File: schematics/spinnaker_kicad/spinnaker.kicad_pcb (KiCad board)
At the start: 2 copper layers, 138 parts, among them J1 Conn_01x02, J2 Conn_01x02, J3 Conn_01x02, J4 Conn_01x02, J5 Jack-DC, J6 Conn_01x08, J7 Conn_01x02, J8 Conn_01x02, J9 Conn_01x02, Q1 AO3401, U1 SpinSemi_FV-1, U10 24LC32, U11 24LC32, U12 24LC32, U13 24LC32, U14 24LC32, U15 24LC32, U16 24LC32, U17 AMS1117-3.3, U18 AMS1117-5.0, U2 TL071, U3 TL071, U4 TL071, U5 TL071, U6 PT2258, U7 MCP4728, U8 PCF8574, U9 24LC32, Y1 32768Hz

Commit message: Corrección de conexiones no enrutadas
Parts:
- removed J7, J8, J9: Conn_01x02, Connector_JST:JST_GH_BM02B-GHS-TBT_1x02-1MP_P1.25mm_Vertical
- added REF**: MountingHole_2.5mm_Pad_Via, MountingHole:MountingHole_2.5mm_Pad_Via, F.Cu at (107.3, 64.1)
- added REF**: MountingHole_2.5mm_Pad_Via, MountingHole:MountingHole_2.5mm_Pad_Via, F.Cu at (107.3, 112.4)
- added REF**: MountingHole_2.5mm_Pad_Via, MountingHole:MountingHole_2.5mm_Pad_Via, F.Cu at (181.0, 112.4)
- added REF**: MountingHole_2.5mm_Pad_Via, MountingHole:MountingHole_2.5mm_Pad_Via, F.Cu at (181.0, 63.5)
- C44, C45, C46, C47, C48, C49, C50, C51, C52, C53, C55, C56, C57, C59, C60: moved to B.Cu
- D1: footprint LED_THT:LED_Rectangular_W3.0mm_H2.0mm -> Connector_Wire:SolderWire-0.75sqmm_1x02_P4.8mm_D1.25mm_OD2.3mm
- J1, J2, J3, J4: footprint Connectors:1X02_LONGPADS -> Connector_Wire:SolderWire-0.75sqmm_1x02_P4.8mm_D1.25mm_OD2.3mm
- J5: value Jack-DC -> Conn_01x02; footprint Connector_BarrelJack:BarrelJack_Horizontal -> Connector_JST:JST_PH_S2B-PH-SM4-TB_1x02-1MP_P2.00mm_Horizontal
- J6: value Conn_01x08 -> Conn_01x10; footprint Connector_JST:JST_GH_SM08B-GHS-TB_1x08-1MP_P1.25mm_Horizontal -> Connector_JST:JST_SH_SM10B-SRSS-TB_1x10-1MP_P1.00mm_Horizontal
- RV1, RV2: footprint Connectors:1X03_LONGPADS -> Connector_Wire:SolderWire-0.75sqmm_1x02_P4.8mm_D1.25mm_OD2.3mm
- moved R46 95.6 mm to (175.3, 85.7)
- moved C33 95.4 mm to (175.3, 82.5)
- moved Q1 94.4 mm to (174.6, 71.8), turned to 90 degrees
- moved R45 94.4 mm to (170.2, 85.7)
- moved C38 94.2 mm to (170.2, 82.5)
- moved C58 91.6 mm to (175.3, 88.9), turned to 180 degrees
- moved R43 87.1 mm to (170.2, 71.8)
- moved C54 83.1 mm to (170.2, 88.9)
- moved C30 79.2 mm to (172.7, 77.5), turned to 0 degrees
- moved U17 67.8 mm to (172.7, 107.3), turned to 270 degrees
- moved U18 67.7 mm to (172.7, 95.2), turned to 270 degrees
- moved J5 66.5 mm to (172.7, 63.5), turned to 180 degrees
- moved C34 57.1 mm to (170.2, 101.0), turned to 180 degrees
- moved C37 57.1 mm to (175.3, 101.0), turned to 180 degrees
- moved R34 54.0 mm to (160.7, 92.7), turned to 180 degrees
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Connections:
- J6 pad 2: T0 -> +3V3
- J6 pad 3: S2 -> +5V
- J6 pad 4: S1 -> +9V
- J6 pad 5: S0 -> T0
- J6 pad 6: SDA -> S2
- J6 pad 7: SCL -> S1
- J6 pad 8: Earth -> S0
- RV1 pad 1: Net-(R1-Pad1) -> Net-(C5-Pad2)
- RV2 pad 1: Net-(R3-Pad1) -> Net-(C6-Pad2)
- U10 pad 7: Net-(U10-Pad7) -> Earth
- U11 pad 7: Net-(U11-Pad7) -> Earth
- U12 pad 7: Net-(U12-Pad7) -> Earth
- U13 pad 7: Net-(U13-Pad7) -> Earth
- U14 pad 7: Net-(U14-Pad7) -> Earth
- U15 pad 7: Net-(U15-Pad7) -> Earth
- U16 pad 7: Net-(U16-Pad7) -> Earth
- U8 pad 4: Net-(U8-Pad4) -> Net-(U12-Pad1)
- U8 pad 5: Net-(U10-Pad1) -> Net-(U11-Pad1)
- U8 pad 6: Net-(U11-Pad1) -> Net-(U10-Pad1)
- U8 pad 7: Net-(U12-Pad1) -> Net-(U8-Pad7)
- U9 pad 1: Net-(U8-Pad4) -> Net-(U8-Pad7)
- U9 pad 7: Net-(U9-Pad7) -> Earth
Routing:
- net +3V3: track 0.00 -> 276.8 mm, vias 0 -> 20
- net SCL: track 0.00 -> 181.7 mm, vias 0 -> 8
- net +9V: track 0.00 -> 158.5 mm, vias 0 -> 6
- net SDA: track 0.00 -> 154.7 mm, vias 0 -> 7
- net Earth: track 0.00 -> 145.3 mm, vias 0 -> 365
- net 4V5: track 0.00 -> 116.9 mm, vias 0 -> 5
- net +5V: track 0.00 -> 114.2 mm, vias 0 -> 4
- net Net-(U8-Pad7): track 0.00 -> 60.3 mm
- net Net-(U10-Pad1): track 0.00 -> 51.9 mm
- net S0: track 0.00 -> 49.6 mm
- net Net-(U16-Pad1): track 0.00 -> 44.3 mm
- net Net-(U11-Pad1): track 0.00 -> 43.5 mm
- net RIGHT_PREOUT: track 0.00 -> 42.0 mm
- net Net-(C25-Pad1): track 0.00 -> 39.5 mm
- net S2: track 0.00 -> 36.7 mm
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- added copper zone on F.Cu, net Earth
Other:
- board outline added: 83.8 x 59.1 mm

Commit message: Rediseño con SMPS.
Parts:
- removed the REF** at (107.3, 64.1)
- removed the REF** at (107.3, 112.4)
- removed the REF** at (181.0, 112.4)
- removed the REF** at (181.0, 63.5)
- added C61: 100nF, Capacitor_SMD:C_0805_2012Metric, F.Cu at (183.5, 86.4)
- added C62: 22uF, Capacitor_SMD:C_0805_2012Metric, F.Cu at (175.3, 85.7)
- added C63: 100nF, Capacitor_SMD:C_0805_2012Metric, F.Cu at (183.5, 77.5)
- added C64: 22uF, Capacitor_SMD:C_0805_2012Metric, F.Cu at (183.5, 74.9)
- added L1: 6.8uH, Inductor_SMD:L_10.4x10.4_H4.8, F.Cu at (179.7, 93.3)
- added R44: 100K, Resistor_SMD:R_0805_2012Metric, F.Cu at (172.1, 74.9)
- added R48: 40K2, Resistor_SMD:R_0805_2012Metric, F.Cu at (175.9, 77.5)
- added R49: 40K2, Resistor_SMD:R_0805_2012Metric, F.Cu at (175.9, 74.9)
- added R50: 7K68, Resistor_SMD:R_0805_2012Metric, F.Cu at (172.1, 77.5)
- added R51: 4K7, Resistor_SMD:R_0805_2012Metric, B.Cu at (133.3, 81.9)
- added REF**: MountingHole_2.2mm_M2_Pad_Via, MountingHole:MountingHole_2.2mm_M2_Pad_Via, F.Cu at (184.2, 62.2)
- added REF**: MountingHole_2.2mm_M2_Pad_Via, MountingHole:MountingHole_2.2mm_M2_Pad_Via, F.Cu at (184.2, 112.4)
- added REF**: MountingHole_2.2mm_M2_Pad_Via, MountingHole:MountingHole_2.2mm_M2_Pad_Via, F.Cu at (107.3, 112.4)
- added REF**: MountingHole_2.2mm_M2_Pad_Via, MountingHole:MountingHole_2.2mm_M2_Pad_Via, F.Cu at (107.3, 62.2)
- added U19: MP1470, Package_TO_SOT_SMD:TSOT-23-6, F.Cu at (181.6, 81.9)
- C54, C58, U18: moved to B.Cu
- Y1: footprint Crystal:Crystal_SMD_5032-2Pin_5.0x3.2mm -> Crystal:Crystal_SMD_3215-2Pin_3.2x1.5mm
- moved R46 66.7 mm to (109.2, 95.2), turned to 270 degrees
- moved C33 64.8 mm to (111.8, 95.2), turned to 270 degrees
- moved R45 61.1 mm to (109.2, 90.2), turned to 270 degrees
- moved C38 58.9 mm to (111.8, 90.2), turned to 270 degrees
- moved U18 46.6 mm to (130.8, 74.9), turned to 90 degrees
- moved C58 45.0 mm to (130.8, 81.9), turned to 270 degrees
- moved C54 42.5 mm to (128.3, 81.9), turned to 270 degrees
- moved C30 10.8 mm to (181.0, 70.5)
- moved D6 6.63 mm to (149.2, 78.1)
- moved C41 5.85 mm to (139.7, 88.9)
- moved D5 4.26 mm to (149.2, 83.2)
- moved J3 4.26 mm to (111.8, 100.3)
- moved J4 4.26 mm to (111.8, 105.4)
- moved C27 3.70 mm to (149.2, 91.4)
- moved C34 2.69 mm to (172.1, 102.9)
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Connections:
- C34 pad 1: +5V -> Net-(C34-Pad1)
- J6 pad 3: +5V -> Earth
- U17 pad 3: +5V -> Net-(C34-Pad1)
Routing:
- net +5V: track 114.2 -> 24.7 mm, vias 4 -> 1
- net 4V5: track 116.9 -> 65.4 mm, vias 5 -> 4
- net +9V: track 158.5 -> 201.7 mm, vias 6 -> 7
- net Net-(C34-Pad1): track 0.00 -> 37.4 mm, vias 0 -> 2
- net Net-(R44-Pad2): track 0.00 -> 14.7 mm
- net Earth: track 145.3 -> 158.4 mm, vias 365 -> 34
- net Net-(C61-Pad2): track 0.00 -> 13.0 mm
- net Net-(C17-Pad2): track 24.2 -> 16.9 mm, vias 2 -> 0
- net Net-(R48-Pad1): track 0.00 -> 6.58 mm
- net Net-(C19-Pad2): track 6.50 -> 13.1 mm
- net Net-(C61-Pad1): track 0.00 -> 5.29 mm
- net +3V3: track 276.8 -> 271.7 mm, vias 20 -> 18
- net Net-(C40-Pad2): track 7.26 -> 2.64 mm
- net Net-(C21-Pad2): track 21.5 -> 26.0 mm
- net Net-(R48-Pad2): track 0.00 -> 4.47 mm
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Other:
- board size 83.8 x 59.1 mm -> 87 x 60.3 mm

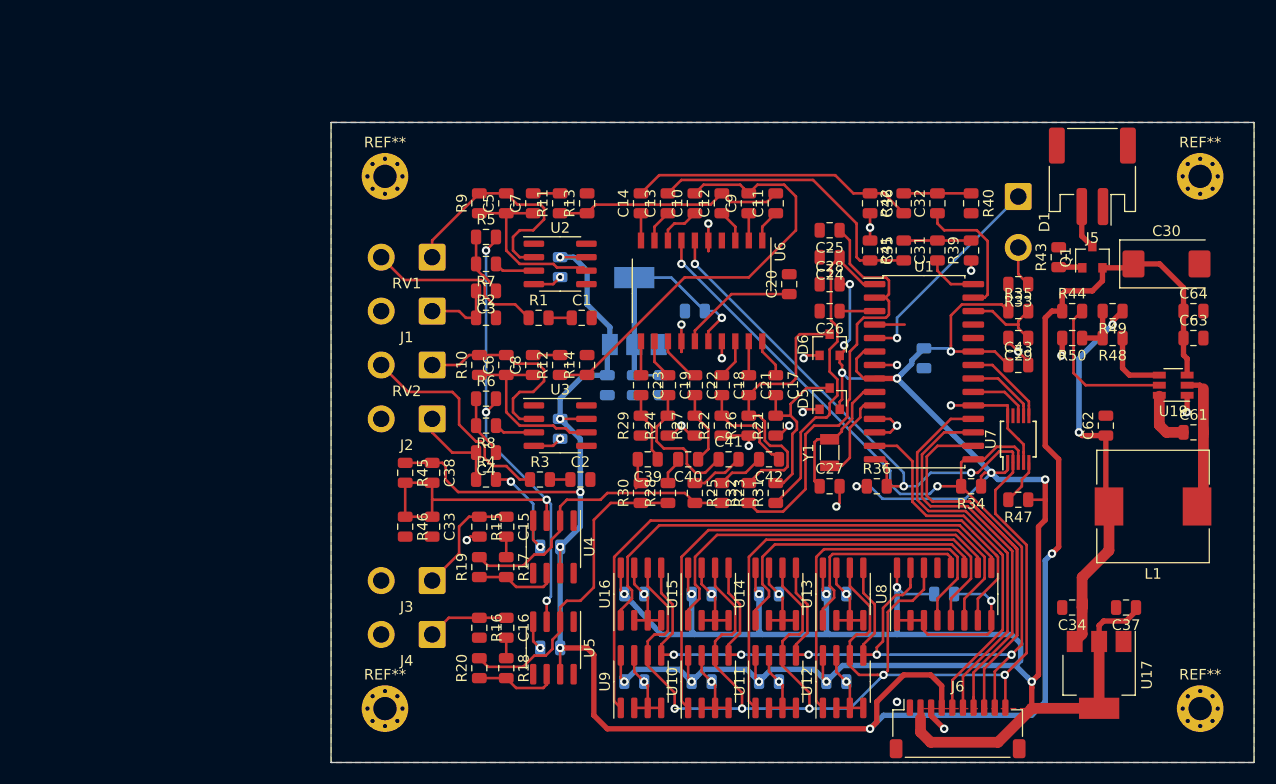
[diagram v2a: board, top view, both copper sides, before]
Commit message: Cambio de conectores a JST-PH. Reducimos alimentación en conector de control a sólo +5VD (SMPS). Otros retoques menores.
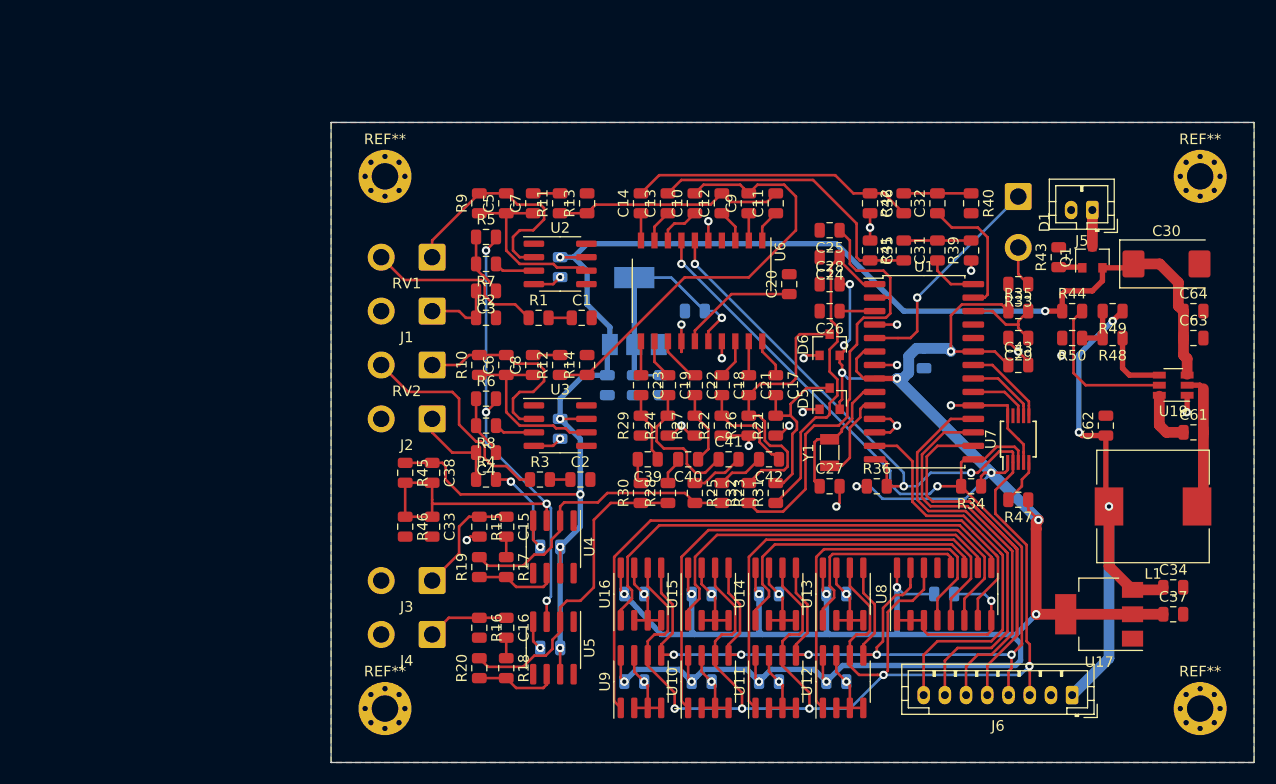
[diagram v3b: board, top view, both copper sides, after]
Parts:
- removed the REF** at (184.2, 62.2)
- removed the REF** at (184.2, 112.4)
- removed the REF** at (107.3, 112.4)
- removed the REF** at (107.3, 62.2)
- added REF**: MountingHole_2.5mm_Pad_Via, MountingHole:MountingHole_2.5mm_Pad_Via, F.Cu at (184.2, 62.2)
- added REF**: MountingHole_2.5mm_Pad_Via, MountingHole:MountingHole_2.5mm_Pad_Via, F.Cu at (107.3, 62.2)
- added REF**: MountingHole_2.5mm_Pad_Via, MountingHole:MountingHole_2.5mm_Pad_Via, F.Cu at (107.3, 112.4)
- added REF**: MountingHole_2.5mm_Pad_Via, MountingHole:MountingHole_2.5mm_Pad_Via, F.Cu at (184.2, 112.4)
- J5: footprint Connector_JST:JST_PH_S2B-PH-SM4-TB_1x02-1MP_P2.00mm_Horizontal -> Connector_JST:JST_PH_B2B-PH-K_1x02_P2.00mm_Vertical
- J6: value Conn_01x10 -> Conn_01x08; footprint Connector_JST:JST_SH_SM10B-SRSS-TB_1x10-1MP_P1.00mm_Horizontal -> Connector_JST:JST_PH_B8B-PH-K_1x08_P2.00mm_Vertical
- moved J6 11.3 mm to (172.1, 111.1), turned to 180 degrees
- moved C34 9.71 mm to (181.6, 101.0), turned to 0 degrees
- moved U17 5.72 mm to (174.6, 103.5), turned to 180 degrees
- moved C37 4.49 mm to (181.6, 103.5), turned to 0 degrees
- moved J5 3.18 mm to (174.0, 65.4)
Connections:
- C34 pad 1: Net-(C34-Pad1) -> +5VD
- C62 pad 1: Net-(C34-Pad1) -> +5VD
- J5 pad 1: Earth -> Net-(J5-Pad1)
- J5 pad 2: Net-(J5-Pad2) -> Earth
- J6 pad 1: Earth -> +5VD
- J6 pad 2: +3V3 -> Earth
- J6 pad 3: Earth -> SCL
- J6 pad 4: +9V -> SDA
- J6 pad 5: T0 -> S0
- J6 pad 6: S2 -> S1
- J6 pad 7: S1 -> S2
- J6 pad 8: S0 -> T0
- L1 pad 2: Net-(C34-Pad1) -> +5VD
- Q1 pad 3: Net-(J5-Pad2) -> Net-(J5-Pad1)
- R49 pad 1: Net-(C34-Pad1) -> +5VD
- U17 pad 3: Net-(C34-Pad1) -> +5VD
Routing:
- net +9V: track 201.7 -> 146.1 mm, vias 7 -> 6
- net +5VD: track 0.00 -> 53.6 mm, vias 0 -> 3
- net Net-(C34-Pad1): track 37.4 -> 0.00 mm, vias 2 -> 0
- net +3V3: track 271.7 -> 240.9 mm
- net Earth: track 158.4 -> 151.7 mm, vias 34 -> 33
- net Net-(J5-Pad2): track 4.18 -> 0.00 mm
- net Net-(J5-Pad1): track 0.00 -> 3.44 mm
- net T0: track 34.9 -> 37.8 mm
- net SDA: track 156.3 -> 154.6 mm
- net Net-(C25-Pad1): track 41.3 -> 42.8 mm
- net S2: track 38.0 -> 39.3 mm
- net S0: track 50.9 -> 49.6 mm
- net Net-(C24-Pad1): track 32.9 -> 31.9 mm
- net Net-(D1-Pad1): track 20.2 -> 20.9 mm
- net SCL: track 184.0 -> 184.8 mm
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
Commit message: Recolocar etiquetas en silkscreen. Añadir logos en silkscreen. Añadir mallado de vías en planos de tierra.
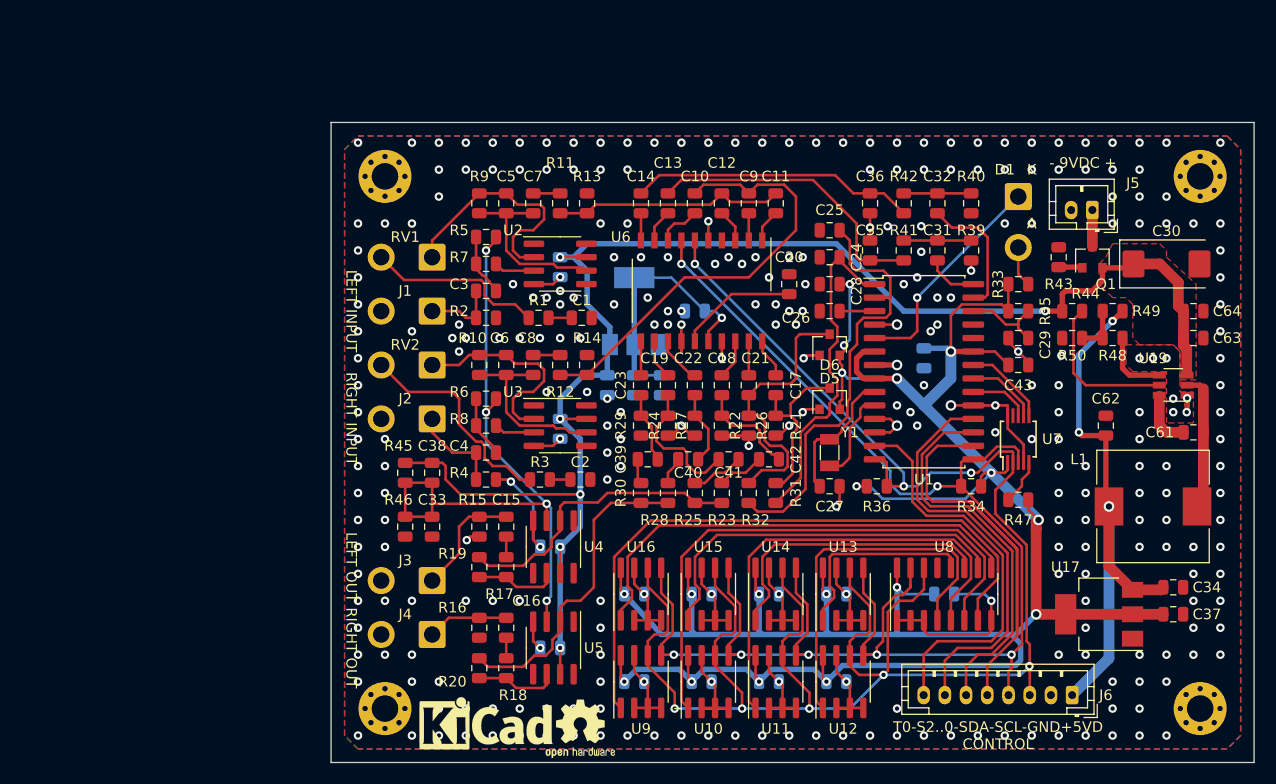
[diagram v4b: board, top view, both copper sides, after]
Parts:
- added REF**: KiCad-Logo_5mm_SilkScreen, Symbol:KiCad-Logo_5mm_SilkScreen, F.Cu at (116.8, 114.3)
- added REF**: OSHW-Logo2_7.3x6mm_SilkScreen, Symbol:OSHW-Logo2_7.3x6mm_SilkScreen, F.Cu at (125.7, 114.3)
- added REF**: KiCad-Logo2_12mm_SilkScreen, Symbol:KiCad-Logo2_12mm_SilkScreen, B.Cu at (148.6, 63.5)
- added REF**: OSHW-Logo_28.5x30mm_SilkScreen, Symbol:OSHW-Logo_28.5x30mm_SilkScreen, B.Cu at (172.7, 83.2)
- J1: value Conn_01x02 -> L_INP
- J2: value Conn_01x02 -> R_INP
- J3: value Conn_01x02 -> L_OUT
- J4: value Conn_01x02 -> R_OUT
- J5: value Conn_01x02 -> 9VDC POWER
- J6: value Conn_01x08 -> CONTROL
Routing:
- net +3V3: track 240.9 -> 242.4 mm
- net Earth: vias 33 -> 298
- added copper zone on F.Cu, net +9V
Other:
- board text added: "- 9VDC +"
- board text added: "A"
- board text added: "K"
- board text added: "LEFT INPUT"
- board text added: "LEFT OUT"
- board text added: "RIGHT INPUT"
- board text added: "RIGHT OUT"
- board text added: "T0-S2..0-SDA-SCL-GND+5VD CONTROL"

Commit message: Pequeños retoques en la PCB (espaciado de pistas, zona de 3V3 para disipar calor, etc...)
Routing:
- net Earth: track 151.7 -> 155.5 mm, vias 298 -> 324
- net T0: track 37.8 -> 36.9 mm
- net Net-(R1-Pad1): track 16.9 -> 17.8 mm
- net S2: track 39.3 -> 38.6 mm
- net Net-(C3-Pad1): track 5.91 -> 6.62 mm
- net S1: track 36.5 -> 36.0 mm
- added copper zone on F.Cu, net +3V3
- added copper zone on F.Cu, net 4V5
- added copper zone on F.Cu, net Net-(C61-Pad2)

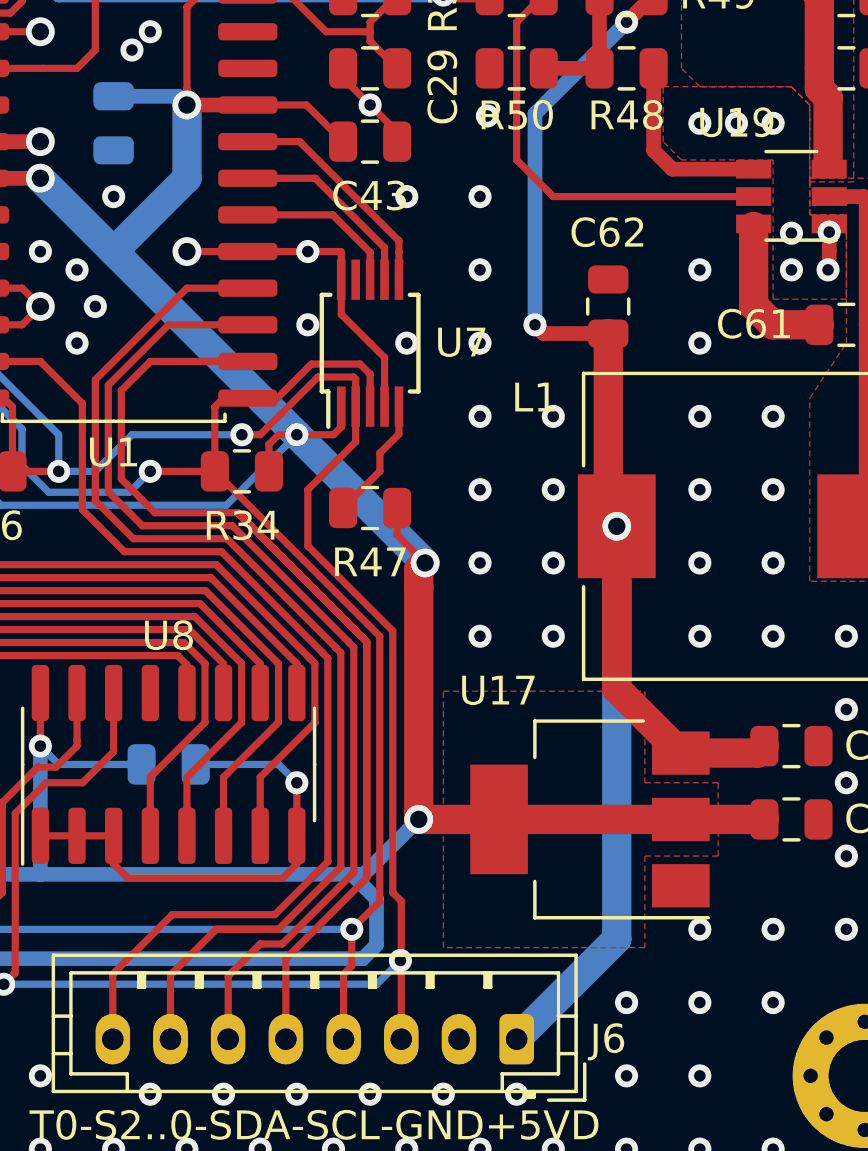
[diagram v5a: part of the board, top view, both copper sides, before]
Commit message: Se añade logo en silkscreen
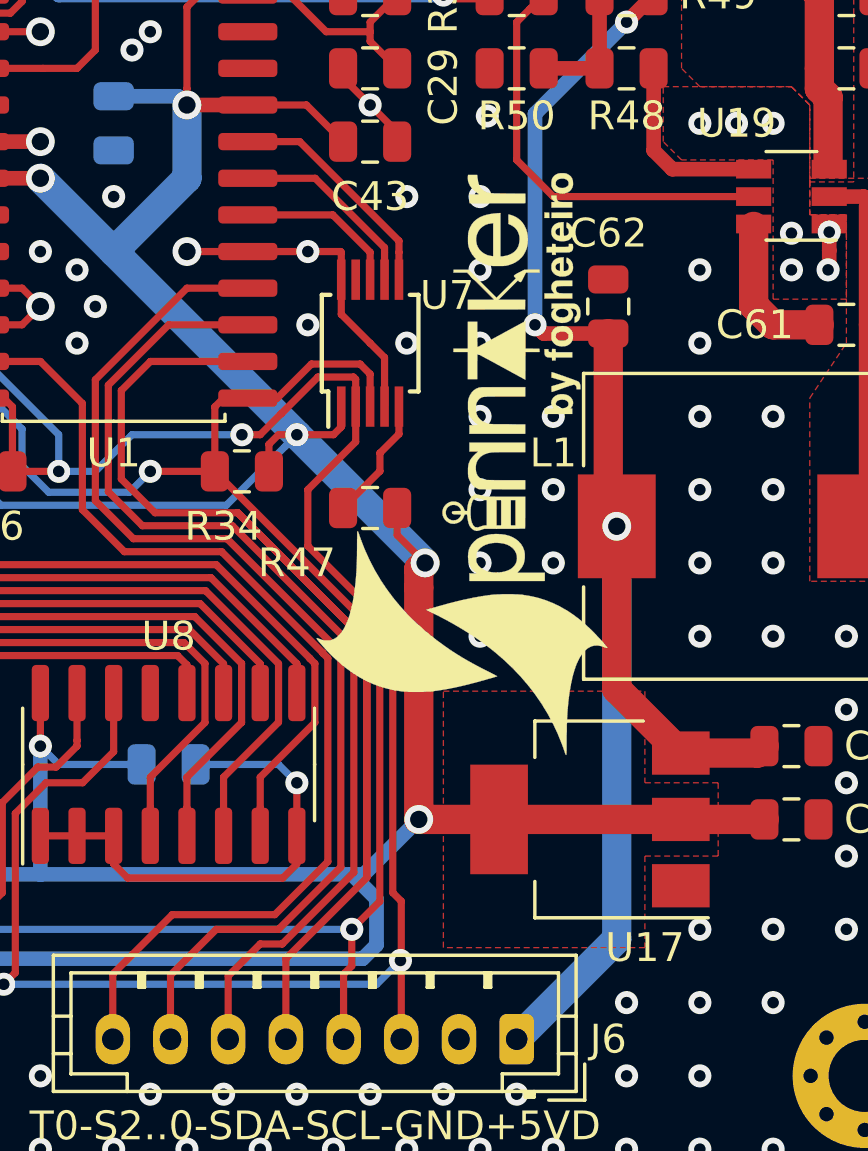
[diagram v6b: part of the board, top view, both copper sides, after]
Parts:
- removed the REF** at (172.7, 83.2)
- added G***: LOGO, logo:spinnaker_logo_silkscreen_20x10mm, F.Cu at (170.2, 91.2)
- added G***: LOGO, logo:spinnaker_logo_silkscreen_50x25mm, B.Cu at (154.3, 88.3)
- added REF**: OSHW-Logo_19x20mm_SilkScreen, Symbol:OSHW-Logo_19x20mm_SilkScreen, B.Cu at (144.1, 73.0)
- moved REF** 17.2 mm to (165.7, 64.1)
